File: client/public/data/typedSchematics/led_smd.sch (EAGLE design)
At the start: 2 parts

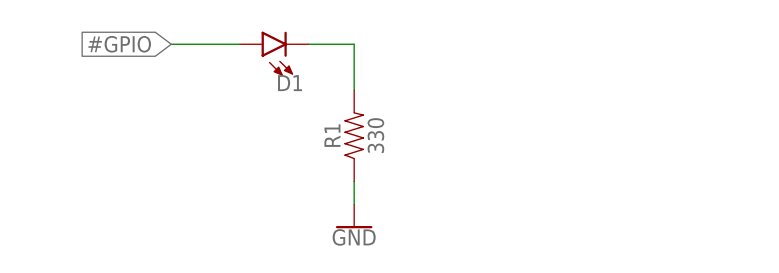
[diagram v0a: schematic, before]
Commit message: Configuring schematics with blocktype info
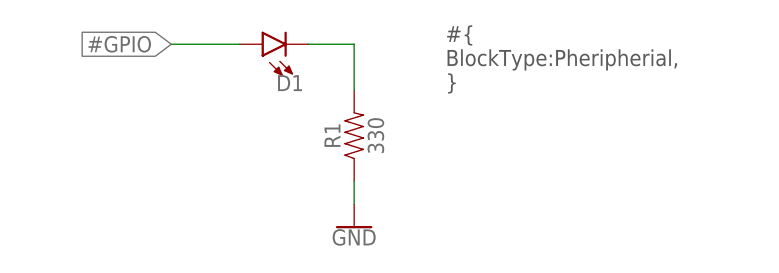
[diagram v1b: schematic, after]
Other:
- note added: "#{ BlockType:Pheripherial, }"
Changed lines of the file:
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@@
 <sheet>
 <plain>
+<text x="20.32" y="-5.08" size="1.778" layer="97">#{
+BlockType:Pheripherial,
+}</text>
 </plain>
 <instances>
@@
 </drawing>
 <compatibility>
+<note version="6.3" minversion="6.2.2" severity="warning">
+Since Version 6.2.2 text objects can contain more than one line,
+which will not be processed correctly with this version.
+</note>
 <note version="8.2" severity="warning">
 Since Version 8.2, EAGLE supports online libraries. The ids

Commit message: Adding GPIO altname for led typed schematic
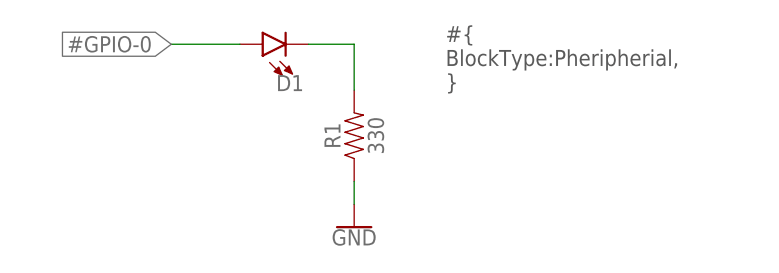
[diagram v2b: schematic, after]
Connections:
- net #GPIO renamed #GPIO-0
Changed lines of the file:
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@@
 </segment>
 </net>
-<net name="#GPIO" class="0">
+<net name="#GPIO-0" class="0">
 <segment>
 <pinref part="D1" gate="G$1" pin="A"/>
